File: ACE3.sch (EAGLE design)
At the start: 140 parts, among them IC1 7805T, Q1 2N3904, Q2 2N3904, Q3 BC237, X1 6M5

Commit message: Correct problem the CNT8 as input for Video Screen Access.
Signed-off-by: John Bradley <flypie@rocketmail.com>
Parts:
- S1: value (none) -> 1
- S10: value (none) -> 0
- S11: value (none) -> Q
- S12: value (none) -> W
- S13: value (none) -> E
- S14: value (none) -> R
- S15: value (none) -> T
- S16: value (none) -> Y
- S17: value (none) -> U
- S18, S27: value (none) -> I
- S19: value (none) -> O
- S2: value (none) -> 2
- S20: value (none) -> P
- S21: value (none) -> A
- S22: value (none) -> S
- S23: value (none) -> D
- S24: value (none) -> F
- S25: value (none) -> G
- S26: value (none) -> H
- S28: value (none) -> J
- S29: value (none) -> K
- S3: value (none) -> 3
- S30: value (none) -> L
- S31: value (none) -> SHIFT
- S32: value (none) -> CTRL
- S33: value (none) -> Z
- S34: value (none) -> X
- S35: value (none) -> C
- S36: value (none) -> V
- S37: value (none) -> B
- S38: value (none) -> N
- S39: value (none) -> M
- S4: value (none) -> 4
- S40: value (none) -> SPACE
- S5: value (none) -> 5
- S6: value (none) -> 6
- S7: value (none) -> 7
- S8: value (none) -> 8
- S9: value (none) -> 9
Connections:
- net CNT12: now also R16.1; no longer R15.1
- net CNT13: now also R17.1; no longer R16.1
- net CNT14: now also R18.1; no longer R17.1
- net CNT15: now also R19.1; no longer R18.1
- net CNT16: now also R20.1; no longer R19.1
- net CNT17: no longer R20.1
- net CNT7: now also R15.1
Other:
- moved on the sheet: R21, R22, R23, RN1A, RN1B, RN1C, RN1D, RN1E, RN1F, RN1G, RN1H, RN2A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

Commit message: Minor changes update  crystal.
Signed-off-by: John Bradley <flypie@rocketmail.com>
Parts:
- X1: value 6M5 -> 6.556MHz; device crystal:HC49GW -> crystal:CRYSTALHC49U-V
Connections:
- net N$36: now also X1.1; no longer X1.2
- net N$47: now also X1.2; no longer X1.1
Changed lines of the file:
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@@
 <?xml version="1.0" encoding="utf-8"?>
 <!DOCTYPE eagle SYSTEM "eagle.dtd">
-<eagle version="9.3.2">
+<eagle version="9.4.0">
 <drawing>
 <settings>
@@
 <part name="R1" library="rcl" library_urn="urn:adsk.eagle:library:334" deviceset="R-EU_" device="0207/2V" package3d_urn="urn:adsk.eagle:package:23490/1" value="47k"/>
 <part name="Q1" library="transistor" library_urn="urn:adsk.eagle:library:402" deviceset="2N3904" device="" package3d_urn="urn:adsk.eagle:package:28523/2"/>
-<part name="X1" library="crystal" library_urn="urn:adsk.eagle:library:204" deviceset="HC49GW" device="" package3d_urn="urn:adsk.eagle:package:12072/1" value="6M5"/>
 <part name="R9" library="rcl" library_urn="urn:adsk.eagle:library:334" deviceset="R-EU_" device="0207/2V" package3d_urn="urn:adsk.eagle:package:23490/1" value="47k"/>
 <part name="P+16" library="supply1" library_urn="urn:adsk.eagle:library:371" deviceset="VCC" device=""/>
@@
 <part name="Z7-8" library="memory-idt" library_urn="urn:adsk.eagle:library:273" deviceset="6116P" device="" package3d_urn="urn:adsk.eagle:package:1009/2"/>
 <part name="SUPPLY26" library="supply2" library_urn="urn:adsk.eagle:library:372" deviceset="GND" device=""/>
+<part name="X1" library="crystal" library_urn="urn:adsk.eagle:library:204" deviceset="CRYSTAL" device="HC49U-V" package3d_urn="urn:adsk.eagle:package:12075/1" value="6.556MHz"/>
 </parts>
 <sheets>
@@
 <attribute name="VALUE" x="182.88" y="-248.92" size="1.778" layer="96"/>
 </instance>
-<instance part="X1" gate="G$1" x="180.34" y="-233.68" smashed="yes">
-<attribute name="NAME" x="182.88" y="-232.664" size="1.778" layer="95"/>
-<attribute name="VALUE" x="182.88" y="-236.22" size="1.778" layer="96"/>
-</instance>
 <instance part="R9" gate="G$1" x="195.58" y="-228.6" smashed="yes" rot="R270">
 <attribute name="NAME" x="197.0786" y="-224.79" size="1.778" layer="95" rot="R270"/>
@@
 <attribute name="VALUE" x="106.045" y="-43.815" size="1.778" layer="96" rot="R270"/>
 </instance>
+<instance part="X1" gate="G$1" x="180.34" y="-233.68" smashed="yes" rot="R180">
+<attribute name="NAME" x="177.8" y="-234.696" size="1.778" layer="95" rot="R180"/>
+<attribute name="VALUE" x="177.8" y="-231.14" size="1.778" layer="96" rot="R180"/>
+</instance>
 </instances>
 <busses>
@@
 <pinref part="C5" gate="G$1" pin="1"/>
 <wire x1="182.88" y1="-233.68" x2="185.42" y2="-233.68" width="0.1524" layer="91"/>
-<pinref part="X1" gate="G$1" pin="2"/>
+<pinref part="X1" gate="G$1" pin="1"/>
 </segment>
 </net>
@@
 <wire x1="175.26" y1="-248.92" x2="175.26" y2="-246.38" width="0.1524" layer="91"/>
 <wire x1="175.26" y1="-233.68" x2="175.26" y2="-241.3" width="0.1524" layer="91"/>
-<pinref part="X1" gate="G$1" pin="1"/>
 <wire x1="175.26" y1="-241.3" x2="175.26" y2="-246.38" width="0.1524" layer="91"/>
 <wire x1="175.26" y1="-233.68" x2="177.8" y2="-233.68" width="0.1524" layer="91"/>
 <junction x="175.26" y="-241.3"/>
 <junction x="175.26" y="-246.38"/>
+<pinref part="X1" gate="G$1" pin="2"/>
 </segment>
 </net>

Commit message: Update after faults pointed out by Claudius. Decoding address from 8k-16k changed. Transistor changed. Minor changed to take advantage of Hex Invert chip and remove cludged inverts.
Signed-off-by: John Bradley <flypie@rocketmail.com>
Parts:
- removed Q2: 2N3904, transistor:2N3904
- removed Z51: 74S00N, 74xx-eu:74S00N
- added IC2: 74HCT04N, 74xx-eu:74HCT04N
- added IC3: 74HCT08N, 74xx-eu:74HCT08N
- added T1: 2N2369, transistor:2N2369
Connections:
- new net N$28: Z22C.I2, Z29A.Y7
- new net N$30: IC2A.O, IC3A.I0
- new net N$66: Z29A.Y2, Z50A.I1
- net /INT: now also IC2D.O; no longer Z19D.O
- net ADDRESS12: now also IC2A.I, IC3B.I0
- net CSB4KV: now also IC2E.I; no longer Z23B.I0
- net GND: now also T1.E; no longer Q2.E
- net N$1: now also Z29A.Y3, Z50A.I2; no longer Z29A.Y2, Z50A.I0
- net N$2: now also IC3A.O; no longer Z29A.Y1
- net N$21: now also IC2E.O; no longer Z23B.O
- net N$23: now also Z29A.Y5; no longer Z29A.Y6
- net N$24: now also T1.C; no longer Q2.C
- net N$25: now also Z29A.Y6; no longer Z29A.Y7
- net N$26: now also T1.B; no longer Q2.B
- net N$29: now also IC2C.I; no longer Z23A.I1
- net N$3: now also Z29A.Y4, Z50A.I3; no longer Z29A.Y3, Z50A.I1
- net N$39: now also IC2C.O; no longer Z23A.O
- net N$50: now also IC2D.I; no longer Z19D.I0
- net N$6: now also IC3A.I1, IC3B.I1, Z29A.Y1; no longer Z29A.Y4, Z50A.I2
- net N$7: now also IC3B.O, Z50A.I0; no longer Z29A.Y5, Z50A.I3
- net N$8: now also IC2B.I; no longer Z51A.I0, Z51A.I1
- net N$9: now also IC2B.O; no longer Z51A.O
- net VCC: no longer Z19D.I1, Z22C.I2, Z23A.I0, Z23B.I1
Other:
- moved on the sheet: C8, Z19D, Z23A, Z23B, Z25C, Z26A, Z26B, Z26C, Z29, Z50A

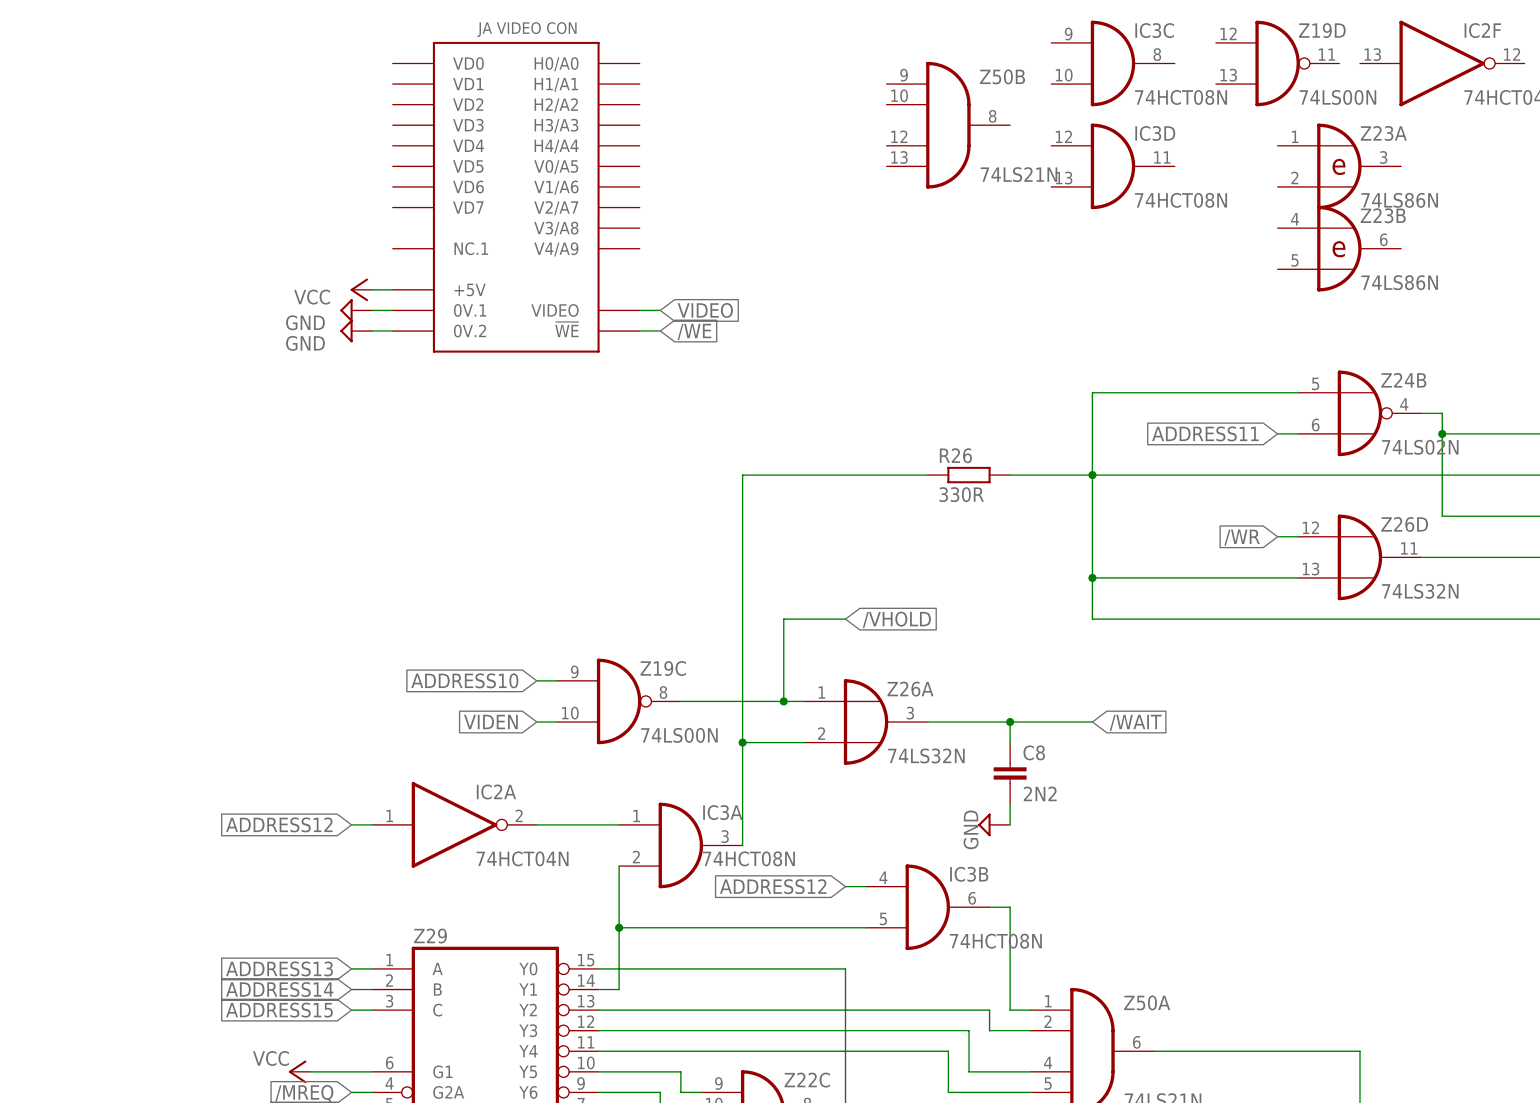
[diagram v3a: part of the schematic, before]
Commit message: Make sure is correct this time. OR not AnD where needed.
Signed-off-by: John Bradley <flypie@rocketmail.com>
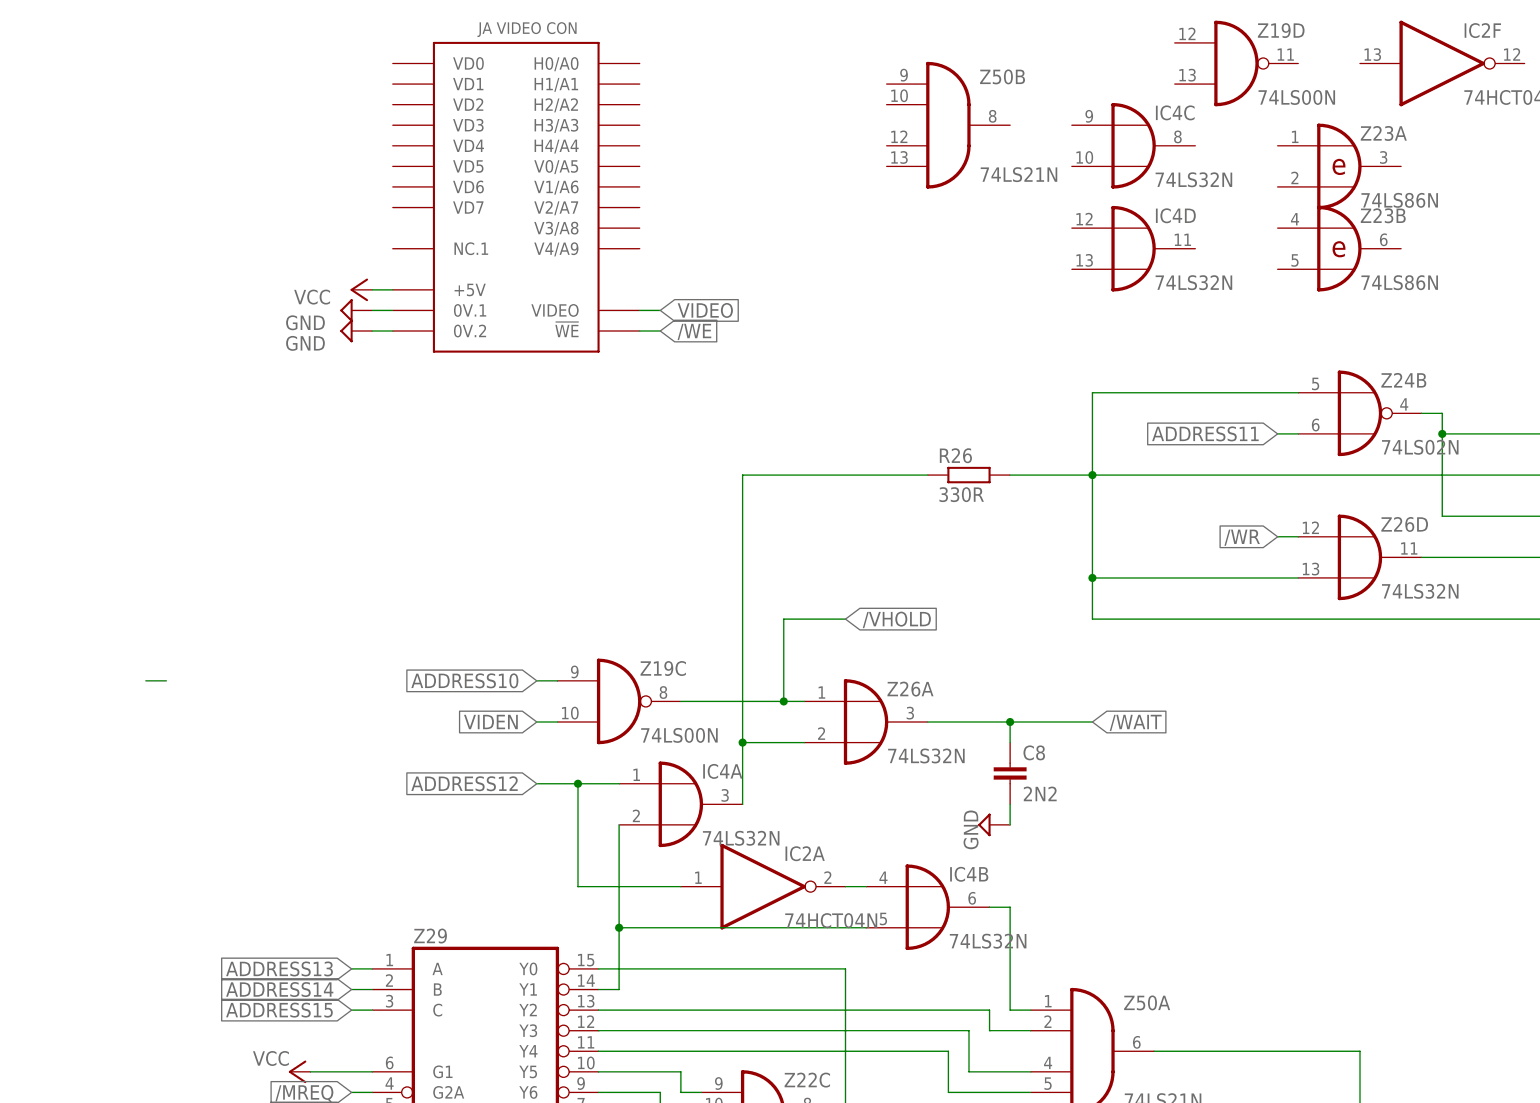
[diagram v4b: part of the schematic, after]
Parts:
- removed IC3: 74HCT08N, 74xx-eu:74HCT08N
- added IC4: 74LS32N, 74xx-eu:74LS32N
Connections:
- net ADDRESS12: now also IC4A.I0; no longer IC3B.I0
- net N$2: now also IC4A.O; no longer IC3A.O
- net N$30: now also IC4B.I0; no longer IC3A.I0
- net N$6: now also IC4A.I1, IC4B.I1; no longer IC3A.I1, IC3B.I1
- net N$7: now also IC4B.O; no longer IC3B.O
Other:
- moved on the sheet: IC2A, Z19D
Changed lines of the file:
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@@
 <part name="X1" library="crystal" library_urn="urn:adsk.eagle:library:204" deviceset="CRYSTAL" device="HC49U-V" package3d_urn="urn:adsk.eagle:package:12075/1" value="6.556MHz"/>
 <part name="IC2" library="74xx-eu" library_urn="urn:adsk.eagle:library:85" deviceset="74*04" device="N" package3d_urn="urn:adsk.eagle:package:16407/2" technology="HCT"/>
-<part name="IC3" library="74xx-eu" library_urn="urn:adsk.eagle:library:85" deviceset="74*08" device="N" package3d_urn="urn:adsk.eagle:package:16407/2" technology="HCT"/>
 <part name="T1" library="transistor" library_urn="urn:adsk.eagle:library:402" deviceset="2N2369" device="" package3d_urn="urn:adsk.eagle:package:28526/2"/>
+<part name="IC4" library="74xx-eu" library_urn="urn:adsk.eagle:library:85" deviceset="74*32" device="N" package3d_urn="urn:adsk.eagle:package:16407/2" technology="LS"/>
 </parts>
 <sheets>
@@
 <attribute name="VALUE" x="177.8" y="-231.14" size="1.778" layer="96" rot="R180"/>
 </instance>
-<instance part="IC2" gate="A" x="-134.62" y="-17.78" smashed="yes">
-<attribute name="NAME" x="-132.08" y="-14.605" size="1.778" layer="95"/>
-<attribute name="VALUE" x="-132.08" y="-22.86" size="1.778" layer="96"/>
-</instance>
 <instance part="IC2" gate="B" x="109.22" y="-25.4" smashed="yes">
 <attribute name="NAME" x="111.76" y="-22.225" size="1.778" layer="95"/>
@@
 <attribute name="VALUE" x="-10.16" y="71.12" size="1.778" layer="96"/>
 </instance>
-<instance part="IC3" gate="A" x="-106.68" y="-20.32" smashed="yes">
-<attribute name="NAME" x="-104.14" y="-17.145" size="1.778" layer="95"/>
-<attribute name="VALUE" x="-104.14" y="-22.86" size="1.778" layer="96"/>
-</instance>
-<instance part="IC3" gate="B" x="-76.2" y="-27.94" smashed="yes">
-<attribute name="NAME" x="-73.66" y="-24.765" size="1.778" layer="95"/>
-<attribute name="VALUE" x="-73.66" y="-33.02" size="1.778" layer="96"/>
-</instance>
-<instance part="IC3" gate="C" x="-53.34" y="76.2" smashed="yes">
-<attribute name="NAME" x="-50.8" y="79.375" size="1.778" layer="95"/>
-<attribute name="VALUE" x="-50.8" y="71.12" size="1.778" layer="96"/>
-</instance>
-<instance part="IC3" gate="D" x="-53.34" y="63.5" smashed="yes">
-<attribute name="NAME" x="-50.8" y="66.675" size="1.778" layer="95"/>
-<attribute name="VALUE" x="-50.8" y="58.42" size="1.778" layer="96"/>
-</instance>
-<instance part="Z19" gate="D" x="-33.02" y="76.2" smashed="yes">
-<attribute name="NAME" x="-30.48" y="79.375" size="1.778" layer="95"/>
-<attribute name="VALUE" x="-30.48" y="71.12" size="1.778" layer="96"/>
+<instance part="Z19" gate="D" x="-38.1" y="76.2" smashed="yes">
+<attribute name="NAME" x="-35.56" y="79.375" size="1.778" layer="95"/>
+<attribute name="VALUE" x="-35.56" y="71.12" size="1.778" layer="96"/>
 </instance>
 <instance part="Z23" gate="A" x="-25.4" y="63.5" smashed="yes">
@@
 <attribute name="VALUE" x="-162.56" y="-152.4" size="1.778" layer="96"/>
 </instance>
+<instance part="IC4" gate="A" x="-106.68" y="-15.24" smashed="yes">
+<attribute name="NAME" x="-104.14" y="-12.065" size="1.778" layer="95"/>
+<attribute name="VALUE" x="-104.14" y="-20.32" size="1.778" layer="96"/>
+</instance>
+<instance part="IC4" gate="B" x="-76.2" y="-27.94" smashed="yes">
+<attribute name="NAME" x="-73.66" y="-24.765" size="1.778" layer="95"/>
+<attribute name="VALUE" x="-73.66" y="-33.02" size="1.778" layer="96"/>
+</instance>
+<instance part="IC4" gate="C" x="-50.8" y="66.04" smashed="yes">
+<attribute name="NAME" x="-48.26" y="69.215" size="1.778" layer="95"/>
+<attribute name="VALUE" x="-48.26" y="60.96" size="1.778" layer="96"/>
+</instance>
+<instance part="IC4" gate="D" x="-50.8" y="53.34" smashed="yes">
+<attribute name="NAME" x="-48.26" y="56.515" size="1.778" layer="95"/>
+<attribute name="VALUE" x="-48.26" y="48.26" size="1.778" layer="96"/>
+</instance>
+<instance part="IC2" gate="A" x="-96.52" y="-25.4" smashed="yes">
+<attribute name="NAME" x="-93.98" y="-22.225" size="1.778" layer="95"/>
+<attribute name="VALUE" x="-93.98" y="-30.48" size="1.778" layer="96"/>
+</instance>
 </instances>
 <busses>
@@
 </segment>
 <segment>
-<label x="-86.36" y="-25.4" size="1.778" layer="95" rot="R180" xref="yes"/>
-<wire x1="-83.82" y1="-25.4" x2="-86.36" y2="-25.4" width="0.1524" layer="91"/>
-<pinref part="IC3" gate="B" pin="I0"/>
-</segment>
-<segment>
-<label x="-147.32" y="-17.78" size="1.778" layer="95" rot="R180" xref="yes"/>
+<wire x1="-124.46" y1="-12.7" x2="-119.38" y2="-12.7" width="0.1524" layer="91"/>
+<pinref part="IC4" gate="A" pin="I0"/>
+<label x="-124.46" y="-12.7" size="1.778" layer="95" rot="R180" xref="yes"/>
+<wire x1="-119.38" y1="-12.7" x2="-114.3" y2="-12.7" width="0.1524" layer="91"/>
+<wire x1="-119.38" y1="-12.7" x2="-119.38" y2="-25.4" width="0.1524" layer="91"/>
+<junction x="-119.38" y="-12.7"/>
 <pinref part="IC2" gate="A" pin="I"/>
-<wire x1="-144.78" y1="-17.78" x2="-147.32" y2="-17.78" width="0.1524" layer="91"/>
+<wire x1="-119.38" y1="-25.4" x2="-106.68" y2="-25.4" width="0.1524" layer="91"/>
 </segment>
 </net>
@@
 <wire x1="-99.06" y1="-7.62" x2="-91.44" y2="-7.62" width="0.1524" layer="91"/>
 <junction x="-99.06" y="-7.62"/>
-<pinref part="IC3" gate="A" pin="O"/>
-<wire x1="-99.06" y1="-20.32" x2="-99.06" y2="-7.62" width="0.1524" layer="91"/>
+<wire x1="-99.06" y1="-15.24" x2="-99.06" y2="-7.62" width="0.1524" layer="91"/>
+<pinref part="IC4" gate="A" pin="O"/>
 </segment>
 </net>
@@
 </segment>
 </net>
-<net name="N$30" class="0">
-<segment>
-<pinref part="IC3" gate="A" pin="I0"/>
-<pinref part="IC2" gate="A" pin="O"/>
-<wire x1="-124.46" y1="-17.78" x2="-114.3" y2="-17.78" width="0.1524" layer="91"/>
-</segment>
-</net>
 <net name="N$1" class="0">
 <segment>
@@
 <segment>
 <wire x1="-114.3" y1="-30.48" x2="-83.82" y2="-30.48" width="0.1524" layer="91"/>
-<pinref part="IC3" gate="B" pin="I1"/>
 <pinref part="Z29" gate="A" pin="Y1"/>
 <wire x1="-116.84" y1="-38.1" x2="-114.3" y2="-38.1" width="0.1524" layer="91"/>
 <wire x1="-114.3" y1="-38.1" x2="-114.3" y2="-30.48" width="0.1524" layer="91"/>
-<pinref part="IC3" gate="A" pin="I1"/>
-<wire x1="-114.3" y1="-30.48" x2="-114.3" y2="-22.86" width="0.1524" layer="91"/>
+<wire x1="-114.3" y1="-30.48" x2="-114.3" y2="-17.78" width="0.1524" layer="91"/>
 <junction x="-114.3" y="-30.48"/>
+<pinref part="IC4" gate="A" pin="I1"/>
+<pinref part="IC4" gate="B" pin="I1"/>
 </segment>
 </net>
 <net name="N$7" class="0">
 <segment>
-<pinref part="IC3" gate="B" pin="O"/>
 <wire x1="-68.58" y1="-27.94" x2="-66.04" y2="-27.94" width="0.1524" layer="91"/>
 <wire x1="-66.04" y1="-27.94" x2="-66.04" y2="-40.64" width="0.1524" layer="91"/>
 <pinref part="Z50" gate="A" pin="I0"/>
 <wire x1="-66.04" y1="-40.64" x2="-63.5" y2="-40.64" width="0.1524" layer="91"/>
+<pinref part="IC4" gate="B" pin="O"/>
 </segment>
 </net>
@@
 </segment>
 </net>
+<net name="N$30" class="0">
+<segment>
+<pinref part="IC4" gate="B" pin="I0"/>
+<wire x1="-83.82" y1="-25.4" x2="-86.36" y2="-25.4" width="0.1524" layer="91"/>
+<pinref part="IC2" gate="A" pin="O"/>
+</segment>
+</net>
+<net name="N$72" class="0">
+<segment>
+<wire x1="-170.18" y1="0" x2="-172.72" y2="0" width="0.1524" layer="91"/>
+</segment>
+</net>

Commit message: Update parts to either LS or HCT if no LS available,  Revert to orginal numbering scheme.
Signed-off-by: John Bradley <flypie@rocketmail.com>
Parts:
- removed JP1, JP2, JP4: 1503_02, con-lumberg:1503_02
- removed JP3: RC-5231, con-lumberg:RC-5231
- added AUDIO-IN, AUDIO-OUT, POWER-9V-DC-IN: 1503_04, con-lumberg:1503_04
- added VIDEO-OUT: WBTOR1, con-lumberg:WBTOR1
- Z14: value 74LS367D -> 74HCT367N; device 74xx-eu:74LS367D -> 74xx-eu:74HCT367N
- Z15, Z16, Z17, Z18: value 74367N -> 74HCT367N; device 74xx-eu:74367N -> 74xx-eu:74HCT367N
- renumbered Z28 to Z12, Z29 to Z13
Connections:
- net GND: now also AUDIO-IN.2, AUDIO-OUT.2, POWER-9V-DC-IN.2, VIDEO-OUT.S; no longer JP1.2, JP2.2, JP3.S, JP4.2
- net N$12: now also AUDIO-IN.1, AUDIO-IN.3; no longer JP4.1, JP4.3
- net N$29: no longer Z14A.1G
- net N$43: now also AUDIO-OUT.1, AUDIO-OUT.3; no longer JP1.1, JP1.3
- net N$65: now also POWER-9V-DC-IN.1, POWER-9V-DC-IN.3; no longer JP2.1, JP2.3
- net VIDEO: now also VIDEO-OUT.T; no longer JP3.T
